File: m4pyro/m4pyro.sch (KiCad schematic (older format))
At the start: 78 parts, among them IC1 MCP2562, J1 WEST TOP, J2 EAST TOP, P1 SWD_TC, Y1 26M

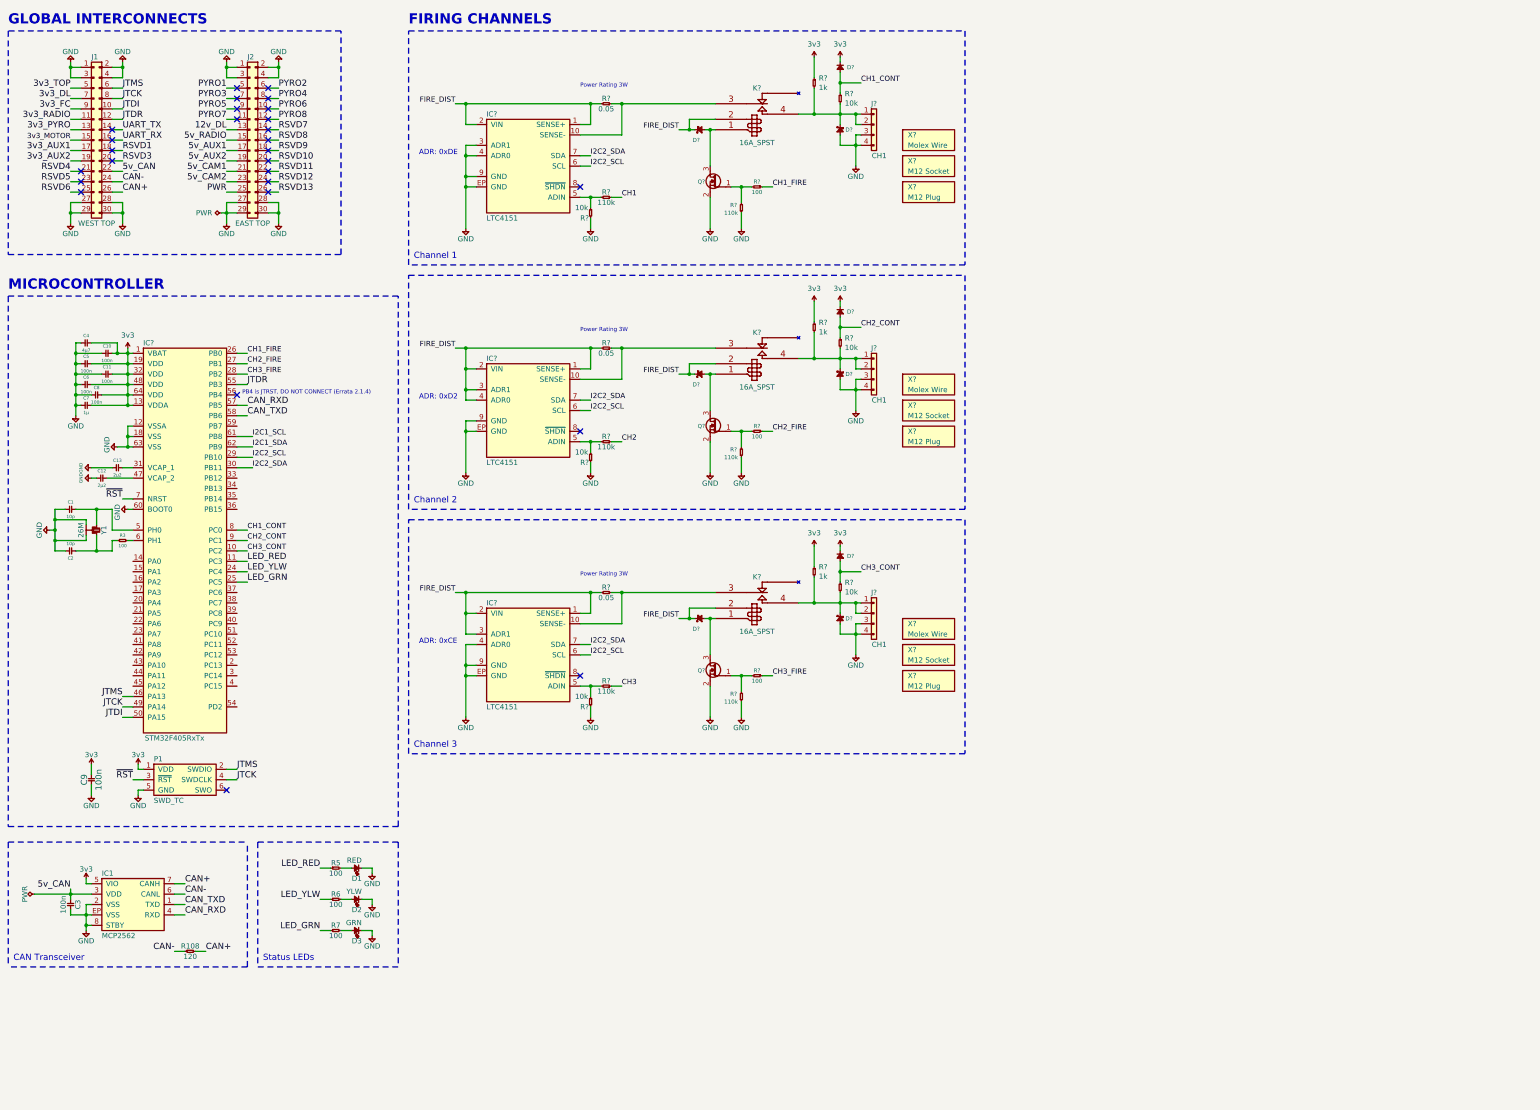
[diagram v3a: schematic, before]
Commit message: Add supply arming
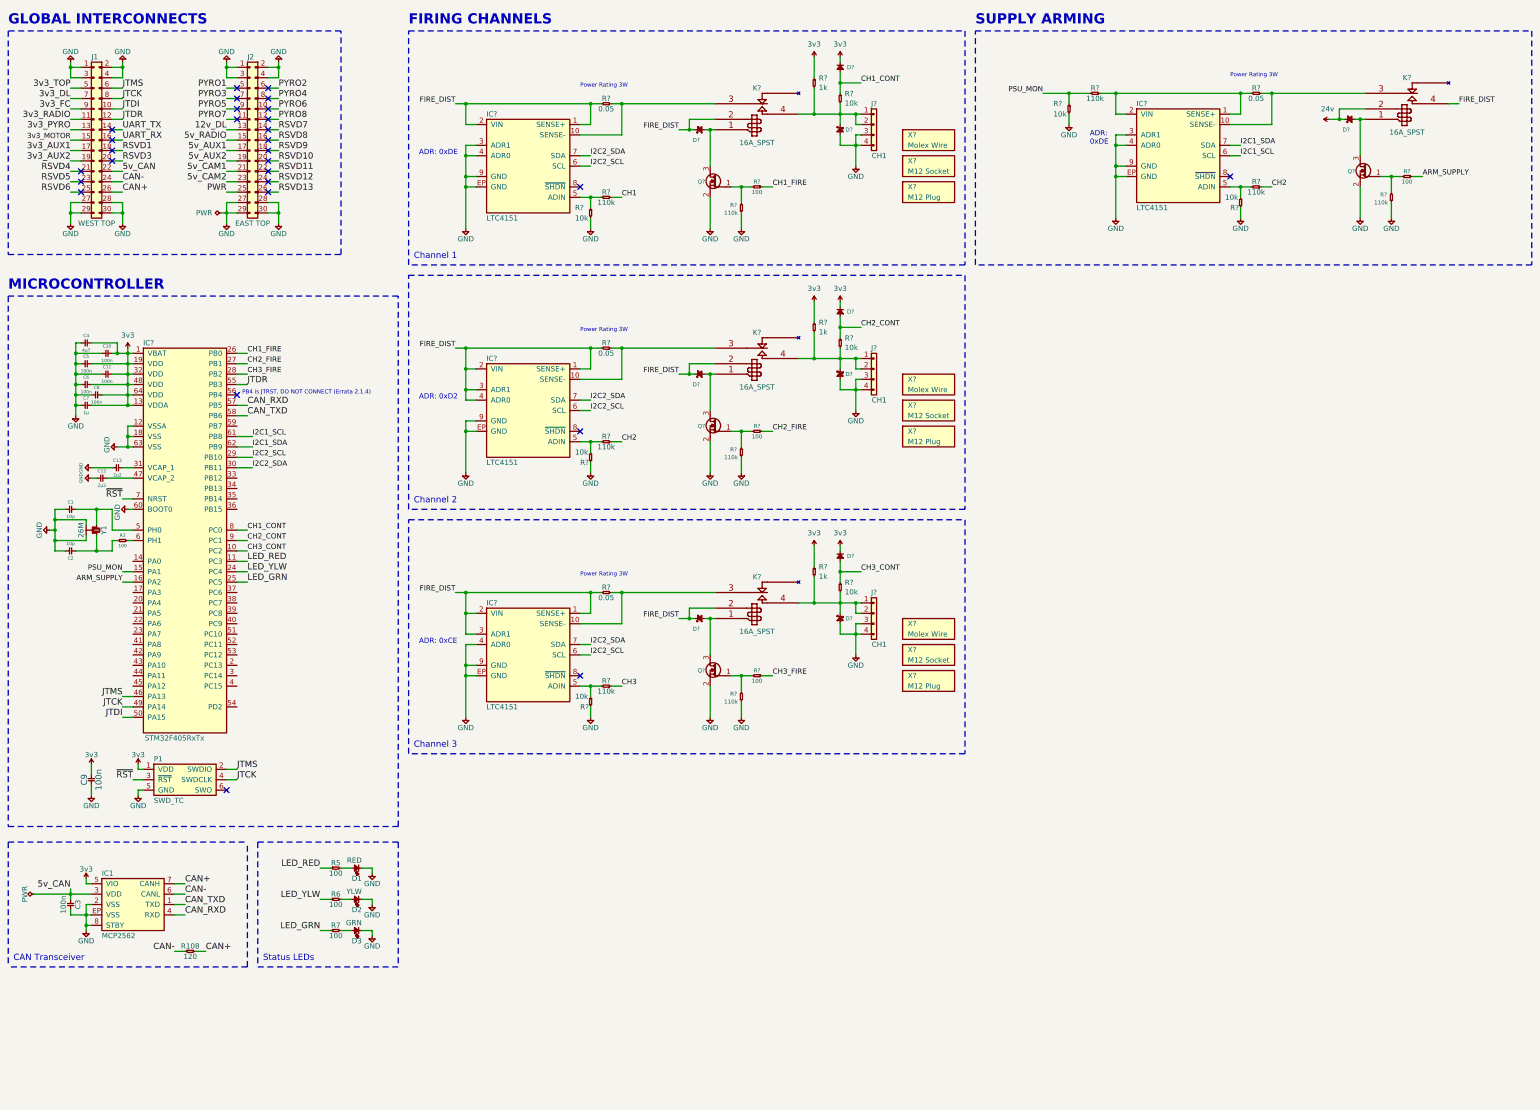
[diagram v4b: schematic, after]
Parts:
- added D?: SCHOTTKY, ignition:SOD-123FL, symbol cusf-kicad:SCHOTTKY
- added IC?: LTC4151, agg:MSOP-10, symbol cusf-kicad:LTC4151
- added K?: 16A_SPST, symbol cusf-kicad:RELAY_SPST
- added Q?: NFET, agg:SOT-23, symbol cusf-kicad:NFET
- added R?: 110k, agg:0603, symbol cusf-kicad:R
- added R?: 100, agg:0603, symbol cusf-kicad:R
- added R? (x2): 110k, symbol cusf-kicad:R
- added R? (x2): 10k, symbol cusf-kicad:R
- added R?: 0.05, symbol cusf-kicad:R
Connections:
- net CH2: now also R?.1
- net FIRE_DIST: now also K?.4
- net GND: now also IC?.3 (ADR1), IC?.4 (ADR0), IC?.9 (GND), IC?.EP (GND), Q?.2 (S), R?.1, R?.2, R?.2
- net I2C1_SCL: now also IC?.6 (SCL)
- net I2C1_SDA: now also IC?.7 (SDA)
- net PSU_MON: now reaches IC?.15 (PA1)
- net PSU_MON: now also R?.1, R?.2
- net ARM_SUPPLY: now reaches IC?.16 (PA2)
- net ARM_SUPPLY: now also R?.1
- new net: IC?.1 (SENSE+), IC?.2 (VIN), R?.1, R?.2
- new net: IC?.10 (SENSE-), K?.3, R?.1
- new net: IC?.5 (ADIN), R?.1, R?.2
- new net: Q?.1 (G), R?.2, R?.2
- new net: D?.2, K?.1, Q?.3 (D)
- new net 24v: D?.1, K?.2
- no-connect marks 27 -> 28
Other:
- note added: "ADR:\n0xDE"
- note added: "SUPPLY ARMING"

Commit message: I2C pullups
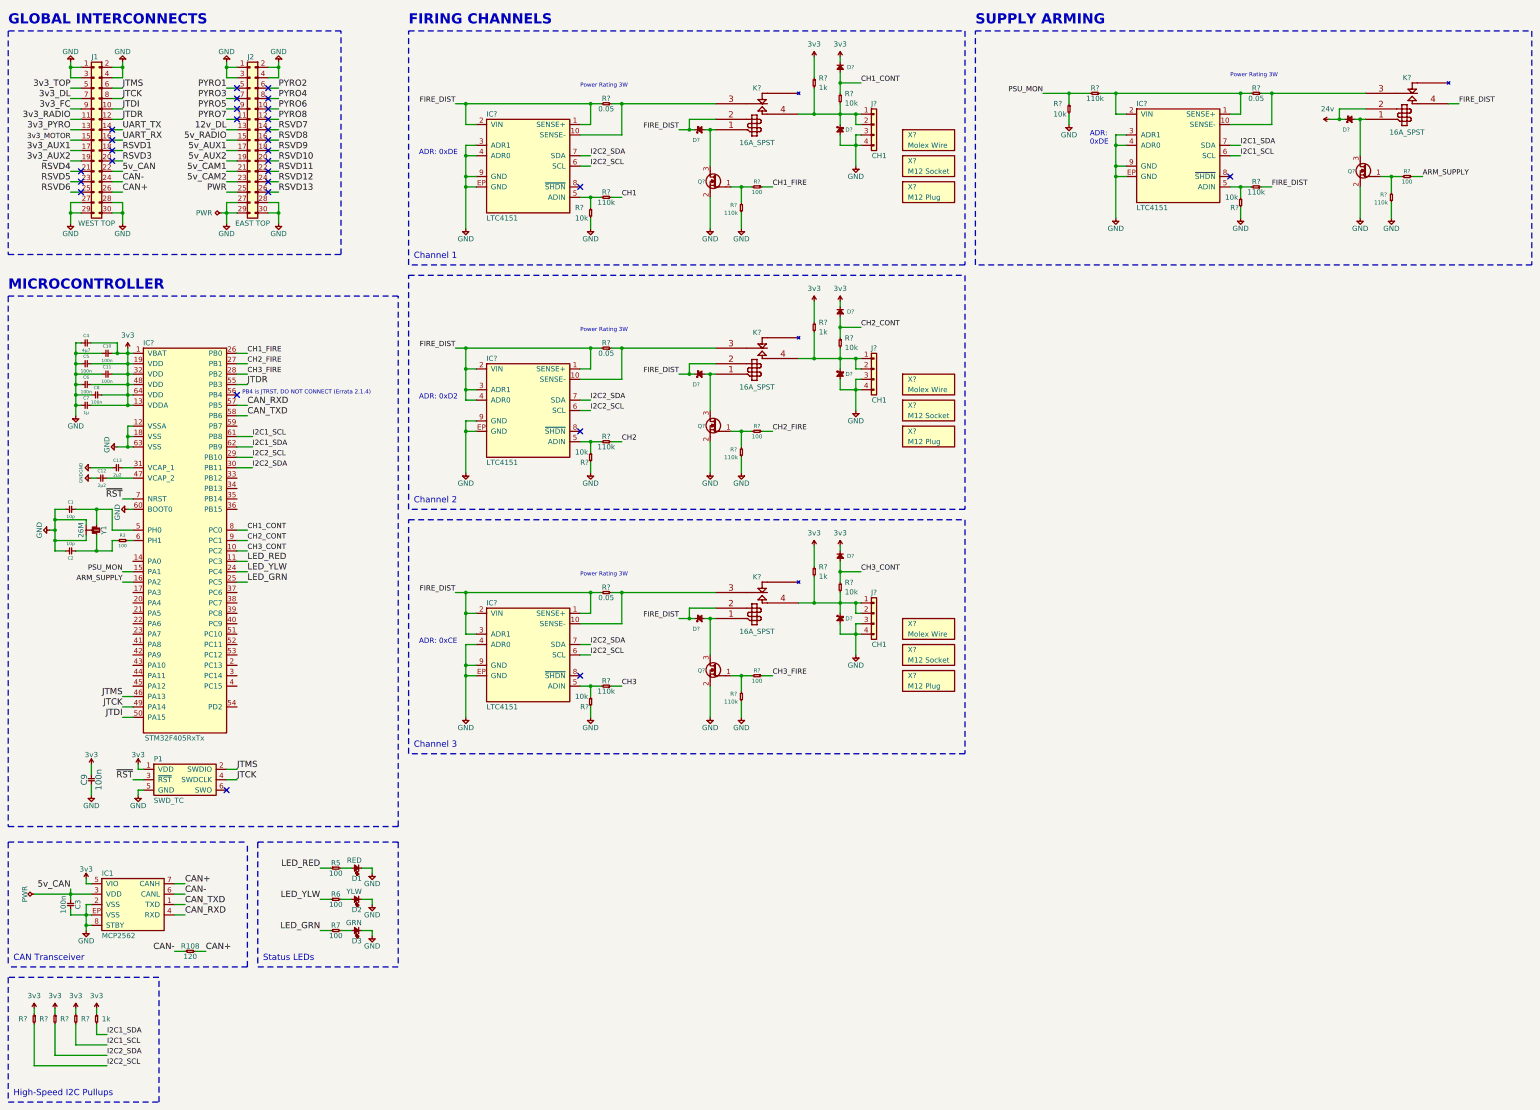
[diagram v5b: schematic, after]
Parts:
- added R? (x4): 1k, symbol cusf-kicad:R
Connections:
- net 3v3: now also R?.1, R?.1, R?.1, R?.1
- net CH2: no longer R?.1
- net FIRE_DIST: now also R?.1
- net I2C1_SCL: now also R?.2
- net I2C1_SDA: now also R?.2
- net I2C2_SCL: now also R?.2
- net I2C2_SDA: now also R?.2
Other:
- note added: "High-Speed I2C Pullups"
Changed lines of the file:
@@
 I2C1_SDA
 Text Label 12800 2300 0    50   ~ 0
-CH2
+FIRE_DIST
 Text Label 14250 2200 0    50   ~ 0
 ARM_SUPPLY
@@
 Text Label 1750 6100 2    50   ~ 0
 ARM_SUPPLY
+$Comp
+L cusf-kicad:3v3 #PWR?
+U 1 1 5FA6F904
+P 900 10200
+F 0 "#PWR?" H 900 10310 50  0001 L CNN
+F 1 "3v3" H 900 10323 50  0000 C CNN
+F 2 "" H 900 10200 50  0001 C CNN
+F 3 "" H 900 10200 50  0001 C CNN
+	1    900  10200
+	1    0    0    -1
+$EndComp
+$Comp
+L cusf-kicad:3v3 #PWR?
+U 1 1 5FA709EC
+P 1100 10200
+F 0 "#PWR?" H 1100 10310 50  0001 L CNN
+F 1 "3v3" H 1100 10323 50  0000 C CNN
+F 2 "" H 1100 10200 50  0001 C CNN
+F 3 "" H 1100 10200 50  0001 C CNN
+	1    1100 10200
+	1    0    0    -1
+$EndComp
+$Comp
+L cusf-kicad:3v3 #PWR?
+U 1 1 5FA70AC8
+P 1300 10200
+F 0 "#PWR?" H 1300 10310 50  0001 L CNN
+F 1 "3v3" H 1300 10323 50  0000 C CNN
+F 2 "" H 1300 10200 50  0001 C CNN
+F 3 "" H 1300 10200 50  0001 C CNN
+	1    1300 10200
+	1    0    0    -1
+$EndComp
+$Comp
+L cusf-kicad:3v3 #PWR?
+U 1 1 5FA70B91
+P 1500 10200
+F 0 "#PWR?" H 1500 10310 50  0001 L CNN
+F 1 "3v3" H 1500 10323 50  0000 C CNN
+F 2 "" H 1500 10200 50  0001 C CNN
+F 3 "" H 1500 10200 50  0001 C CNN
+	1    1500 10200
+	1    0    0    -1
+$EndComp
+$Comp
+L cusf-kicad:R R?
+U 1 1 5FA70D10
+P 1500 10250
+F 0 "R?" V 1550 10100 50  0000 L CNN
+F 1 "1k" V 1550 10300 50  0000 L CNN
+F 2 "" H 1500 10250 50  0001 C CNN
+F 3 "" H 1500 10250 50  0001 C CNN
+	1    1500 10250
+	0    1    1    0
+$EndComp
+$Comp
+L cusf-kicad:R R?
+U 1 1 5FA7272B
+P 1300 10250
+F 0 "R?" V 1350 10100 50  0000 L CNN
+F 1 "1k" V 1350 10350 50  0001 L CNN
+F 2 "" H 1300 10250 50  0001 C CNN
+F 3 "" H 1300 10250 50  0001 C CNN
+	1    1300 10250
+	0    1    1    0
+$EndComp
+$Comp
+L cusf-kicad:R R?
+U 1 1 5FA72D90
+P 1100 10250
+F 0 "R?" V 1150 10100 50  0000 L CNN
+F 1 "1k" V 1150 10350 50  0001 L CNN
+F 2 "" H 1100 10250 50  0001 C CNN
+F 3 "" H 1100 10250 50  0001 C CNN
+	1    1100 10250
+	0    1    1    0
+$EndComp
+$Comp
+L cusf-kicad:R R?
+U 1 1 5FA7303E
+P 900 10250
+F 0 "R?" V 950 10100 50  0000 L CNN
+F 1 "1k" V 950 10350 50  0001 L CNN
+F 2 "" H 900 10250 50  0001 C CNN
+F 3 "" H 900 10250 50  0001 C CNN
+	1    900  10250
+	0    1    1    0
+$EndComp
+Wire Wire Line
+	900  10250 900  10200
+Wire Wire Line
+	1100 10200 1100 10250
+Wire Wire Line
+	1300 10250 1300 10200
+Wire Wire Line
+	1500 10250 1500 10200
+Wire Wire Line
+	1500 10350 1500 10450
+Wire Wire Line
+	1500 10450 1600 10450
+Wire Wire Line
+	1600 10550 1300 10550
+Wire Wire Line
+	1300 10550 1300 10350
+Wire Wire Line
+	1600 10650 1100 10650
+Wire Wire Line
+	1100 10650 1100 10350
+Wire Wire Line
+	1600 10750 900  10750
+Wire Wire Line
+	900  10750 900  10350
+Text Label 1600 10450 0    50   ~ 0
+I2C1_SDA
+Text Label 1600 10550 0    50   ~ 0
+I2C1_SCL
+Text Label 1600 10650 0    50   ~ 0
+I2C2_SDA
+Text Label 1600 10750 0    50   ~ 0
+I2C2_SCL
+Wire Notes Line
+	650  9900 650  11100
+Wire Notes Line
+	650  11100 2100 11100
+Wire Notes Line
+	2100 11100 2100 9900
+Wire Notes Line
+	2100 9900 650  9900
+Text Notes 700  11050 0    60   ~ 0
+High-Speed I2C Pullups
 $EndSCHEMATC

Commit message: Minor layout changes
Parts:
- removed R? (x2): 10k, symbol cusf-kicad:R
- added R? (x2): 10k, symbol cusf-kicad:R
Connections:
- net GND: now also R?.2, R?.2
- net at IC?.5 (ADIN), R?.2: now also R?.1 (x2)
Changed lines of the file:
@@
 P 1050 5600
 F 0 "#PWR01" H 920 5640 50  0001 L CNN
-F 1 "GND" H 1050 5500 50  0000 C CNN
+F 1 "GND" H 1050 5500 31  0000 C CNN
 F 2 "" H 1050 5600 60  0000 C CNN
 F 3 "" H 1050 5600 60  0000 C CNN
@@
 P 1800 5400
 F 0 "#PWR?" H 1670 5440 50  0001 L CNN
-F 1 "GND" H 1750 5300 50  0000 L CNN
+F 1 "GND" V 1850 5300 31  0000 L CNN
 F 2 "" H 1800 5400 50  0001 C CNN
 F 3 "" H 1800 5400 50  0001 C CNN
@@
 P 1700 4800
 F 0 "#PWR?" H 1570 4840 50  0001 L CNN
-F 1 "GND" H 1600 4700 50  0000 L CNN
+F 1 "GND" V 1750 4700 31  0000 L CNN
 F 2 "" H 1700 4800 50  0001 C CNN
 F 3 "" H 1700 4800 50  0001 C CNN
@@
 P 1300 4500
 F 0 "#PWR?" H 1170 4540 50  0001 L CNN
-F 1 "GND" H 1300 4400 50  0000 C CNN
+F 1 "GND" H 1300 4400 31  0000 C CNN
 F 2 "" H 1300 4500 50  0001 C CNN
 F 3 "" H 1300 4500 50  0001 C CNN
@@
 U 1 1 5F584DED
 P 6250 4850
-F 0 "R?" V 6350 4750 50  0000 L CNN
-F 1 "10k" V 6250 4700 50  0000 L CNN
+F 0 "R?" V 6250 4700 50  0000 L CNN
+F 1 "10k" V 6350 4700 50  0000 L CNN
 F 2 "" H 6250 4850 50  0001 C CNN
 F 3 "" H 6250 4850 50  0001 C CNN
@@
 Wire Wire Line
 	6450 7100 6550 7100
-$Comp
-L cusf-kicad:R R?
-U 1 1 5F5E590E
-P 6250 7200
-F 0 "R?" V 6350 7100 50  0000 L CNN
-F 1 "10k" V 6250 7050 50  0000 L CNN
-F 2 "" H 6250 7200 50  0001 C CNN
-F 3 "" H 6250 7200 50  0001 C CNN
-	1    6250 7200
-	0    1    1    0
-$EndComp
 Wire Wire Line
 	5150 7000 5050 7000
@@
 Wire Wire Line
 	12700 2300 12800 2300
-$Comp
-L cusf-kicad:R R?
-U 1 1 5F797F6A
-P 12500 2400
-F 0 "R?" V 12600 2300 50  0000 L CNN
-F 1 "10k" V 12500 2250 50  0000 L CNN
-F 2 "" H 12500 2400 50  0001 C CNN
-F 3 "" H 12500 2400 50  0001 C CNN
-	1    12500 2400
-	0    1    1    0
-$EndComp
 Wire Wire Line
 	11400 2200 11300 2200
@@
 Text Notes 700  11050 0    60   ~ 0
 High-Speed I2C Pullups
+$Comp
+L cusf-kicad:R R?
+U 1 1 5EC9F2D2
+P 6250 7200
+F 0 "R?" V 6250 7050 50  0000 L CNN
+F 1 "10k" V 6350 7050 50  0000 L CNN
+F 2 "" H 6250 7200 50  0001 C CNN
+F 3 "" H 6250 7200 50  0001 C CNN
+	1    6250 7200
+	0    1    1    0
+$EndComp
+$Comp
+L cusf-kicad:R R?
+U 1 1 5ECCF527
+P 12500 2400
+F 0 "R?" V 12500 2250 50  0000 L CNN
+F 1 "10k" V 12600 2250 50  0000 L CNN
+F 2 "" H 12500 2400 50  0001 C CNN
+F 3 "" H 12500 2400 50  0001 C CNN
+	1    12500 2400
+	0    1    1    0
+$EndComp
 $EndSCHEMATC
